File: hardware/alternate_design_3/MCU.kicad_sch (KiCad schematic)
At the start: 1 part, among them U1 NUCLEO64-F411RE

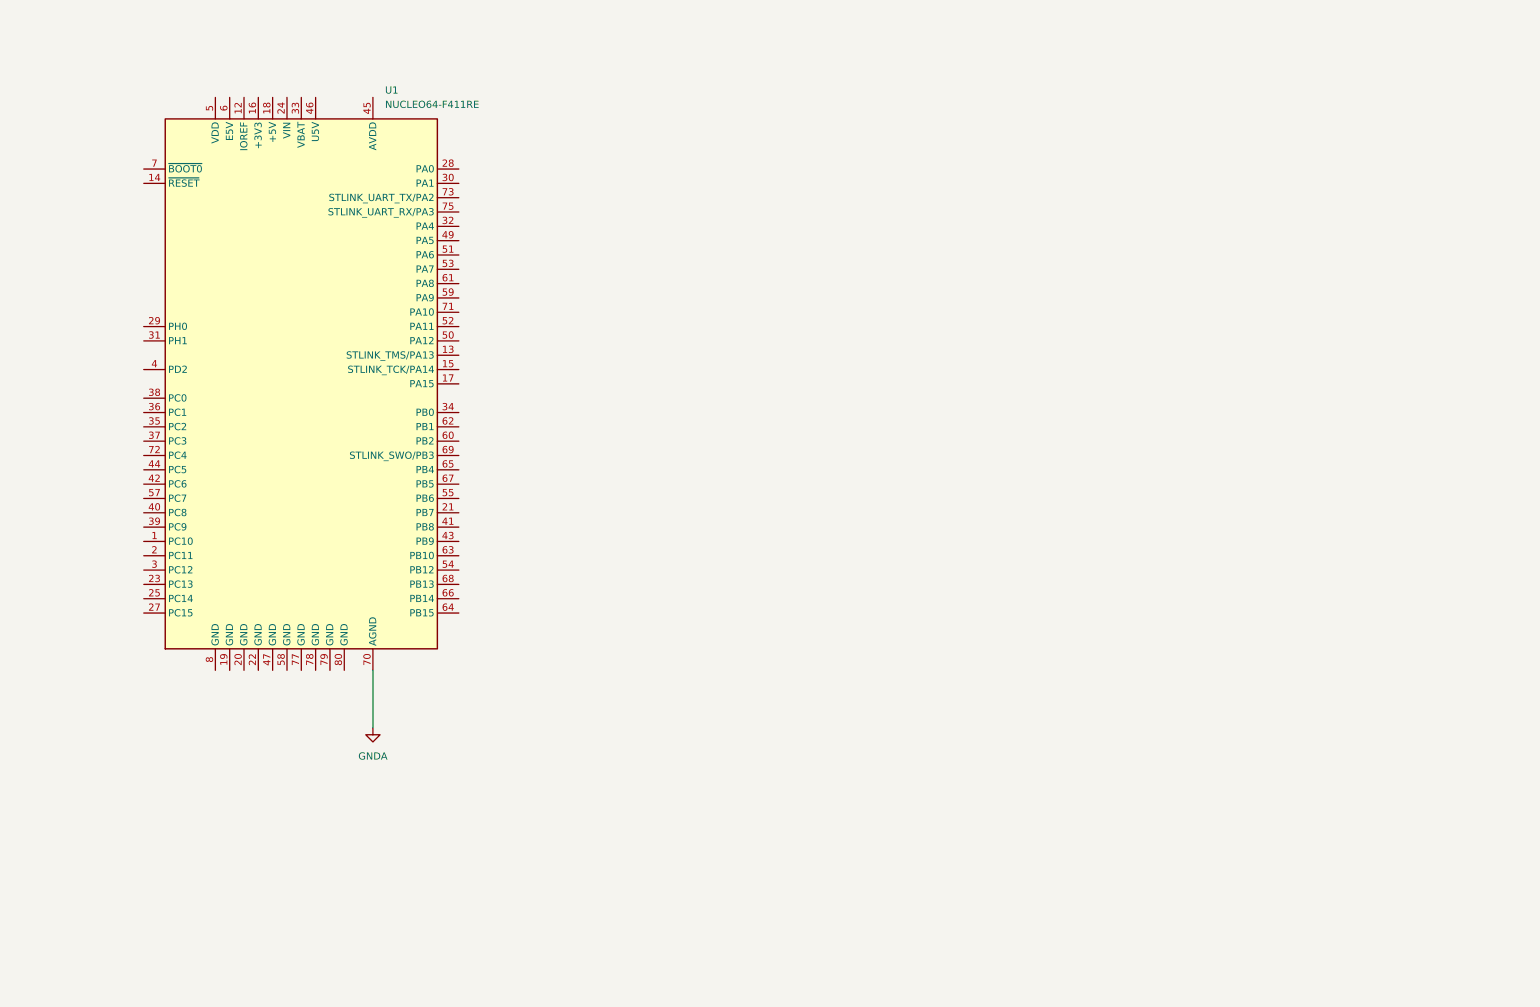
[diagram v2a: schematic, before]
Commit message: major additions to schematic of inverter
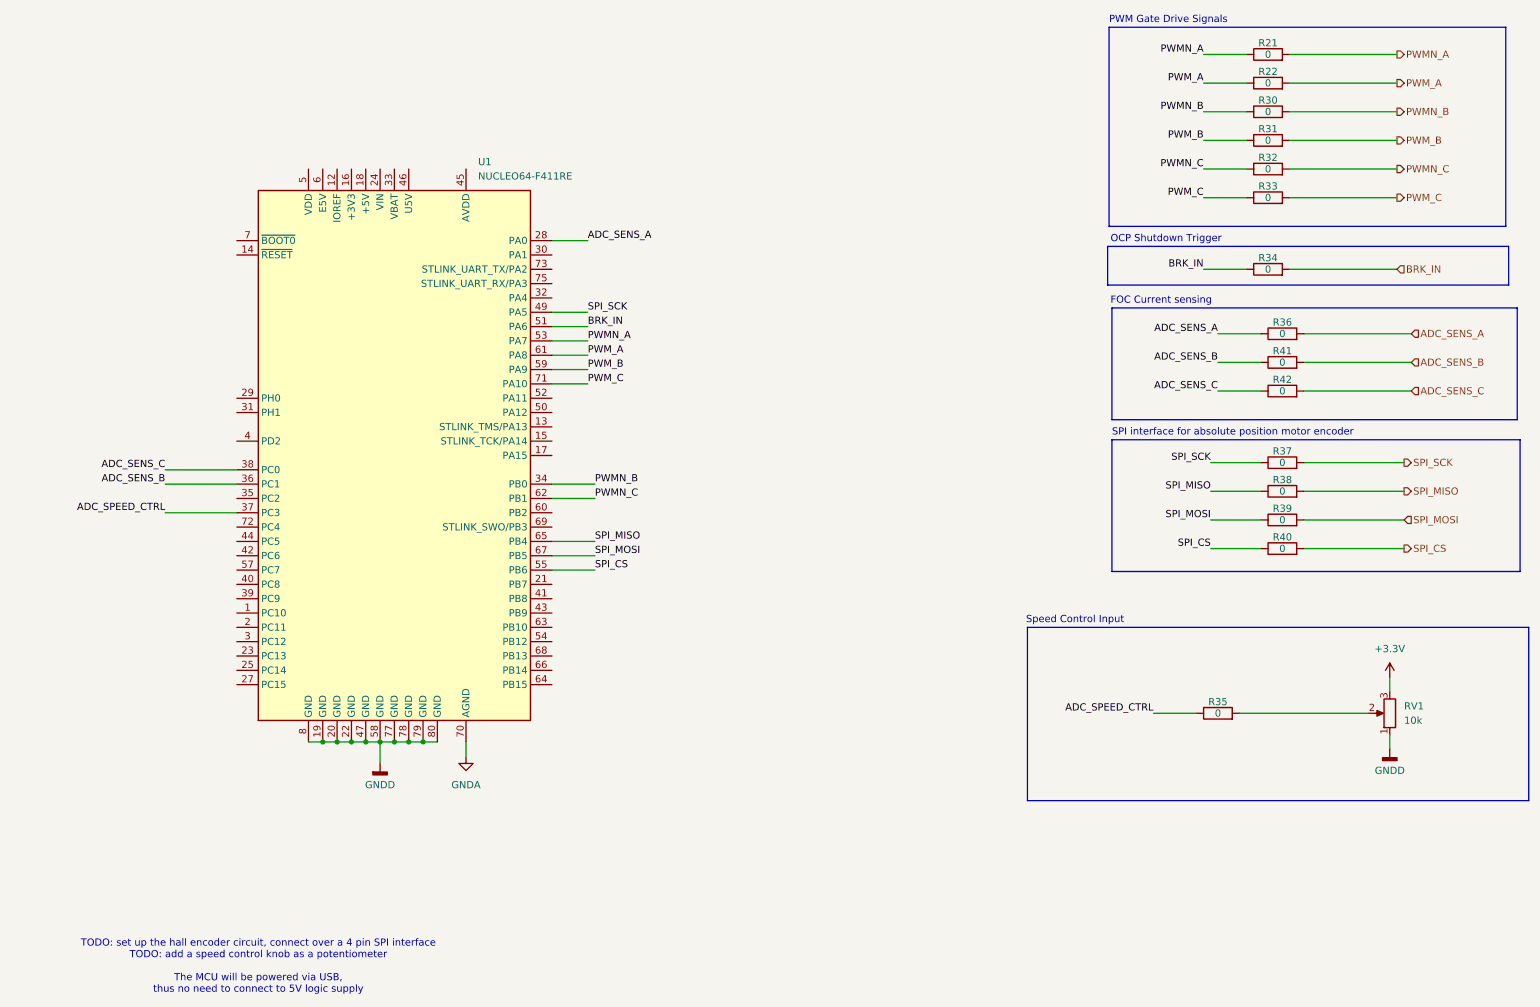
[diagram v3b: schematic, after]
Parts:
- added R21, R22, R30, R31, R32, R33, R34, R35, R36, R37, R38, R39, R40, R41, R42: 0, symbol Device:R
- added RV1: 10k, symbol Device:R_Potentiometer
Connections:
- net GNDD: now reaches U1.19 (GND)
- net GNDD: now also U1.20 (GND), U1.22 (GND), U1.47 (GND), U1.58 (GND), U1.77 (GND), U1.78 (GND), U1.79 (GND), U1.8 (GND), U1.80 (GND), RV1.1
- net ADC_SENS_A: now reaches U1.28 (PA0)
- net ADC_SENS_A: now also R36.1, R36.2
- net PWMN_B: now reaches U1.34 (PB0)
- net PWMN_B: now also R30.1, R30.2
- net ADC_SENS_B: now reaches U1.36 (PC1)
- net ADC_SENS_B: now also R41.1, R41.2
- net ADC_SPEED_CTRL: now reaches U1.37 (PC3)
- net ADC_SPEED_CTRL: now also R35.1
- net ADC_SENS_C: now reaches U1.38 (PC0)
- net ADC_SENS_C: now also R42.1, R42.2
- net SPI_SCK: now reaches U1.49 (PA5)
- net SPI_SCK: now also R37.1, R37.2
- net BRK_IN: now reaches U1.51 (PA6)
- net BRK_IN: now also R34.1, R34.2
- net PWMN_A: now reaches U1.53 (PA7)
- net PWMN_A: now also R21.1, R21.2
- net SPI_CS: now reaches U1.55 (PB6)
- net SPI_CS: now also R40.1, R40.2
- net PWM_B: now reaches U1.59 (PA9)
- net PWM_B: now also R31.1, R31.2
- net PWM_A: now reaches U1.61 (PA8)
- net PWM_A: now also R22.1, R22.2
- net PWMN_C: now reaches U1.62 (PB1)
- net PWMN_C: now also R32.1, R32.2
- net SPI_MISO: now reaches U1.65 (PB4)
- net SPI_MISO: now also R38.1, R38.2
- net SPI_MOSI: now reaches U1.67 (PB5)
- net SPI_MOSI: now also R39.1, R39.2
- net PWM_C: now reaches U1.71 (PA10)
- net PWM_C: now also R33.1, R33.2
- new net: R35.2, RV1.2
- new net +3.3V: RV1.3
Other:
- note added: "FOC Current sensing"
- note added: "OCP Shutdown Trigger"
- note added: "PWM Gate Drive Signals"
- note added: "SPI interface for absolute position motor encoder"
- note added: "Speed Control Input"
- note added: "TODO: set up the hall encoder circuit, connect over a 4 pin SPI interface TODO: add a speed control knob as a potentiometer The MCU will be powered via USB, thus no need to connect to 5V logic supply"
- moved on the sheet: U1
